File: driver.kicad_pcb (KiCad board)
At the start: 2 copper layers, 53.8 x 69.1 mm, 47 parts, among them J1 Screw_Terminal_01x02, J2 Conn_02x12_Odd_Even, Q10 Q_NMOS_GDSD, Q11 Q_NMOS_GDSD, Q12 Q_NMOS_GDSD, Q13 Q_NMOS_GDSD, Q14 Q_NMOS_GDSD, Q15 Q_NMOS_GDSD, Q16 Q_NMOS_GDSD, Q17 IRF9Z34 PMOS_DGS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

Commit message: Remove reset button, finalize capacitor sizes
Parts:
- removed R8: 10K, Resistor_SMD:R_0805_2012Metric_Pad1.15x1.40mm_HandSolder
- removed SW1: SW_Push, Button_Switch_SMD:SW_SPST_B3S-1000
- C1: value 0.1uF -> 1uF 25V; footprint Capacitor_SMD:C_1210_3225Metric_Pad1.42x2.65mm_HandSolder -> Capacitor_SMD:C_1206_3216Metric_Pad1.42x1.75mm_HandSolder
- C2: value 1uF -> 47uF 60V; footprint Capacitor_THT:CP_Radial_D8.0mm_P3.80mm -> Capacitor_THT:CP_Radial_D6.3mm_P2.50mm
- C3: value 1uF 60V -> 47uF 60V; footprint Capacitor_THT:CP_Radial_D8.0mm_P3.80mm -> Capacitor_THT:CP_Radial_D6.3mm_P2.50mm
- moved C3 3.18 mm to (86.4, 79.5), turned to 90 degrees
- moved C1 2.87 mm to (113.5, 83.8), turned to 180 degrees
- moved C2 0.80 mm to (123.4, 79.5)
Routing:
- net VCC: track 98.7 -> 90.5 mm, vias 0 -> 1
- net 28V: track 103.8 -> 106.0 mm

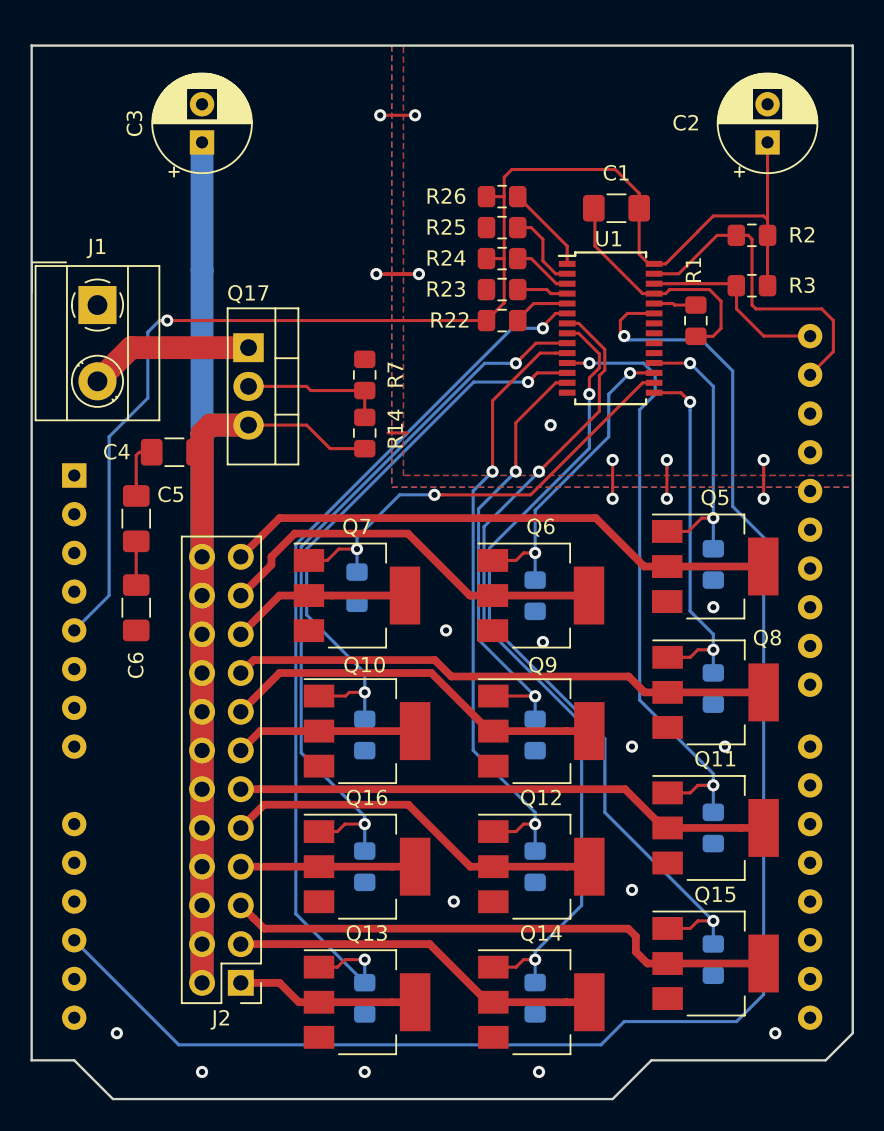
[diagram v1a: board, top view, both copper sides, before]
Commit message: resistor value/footprint changes and associated routing changes
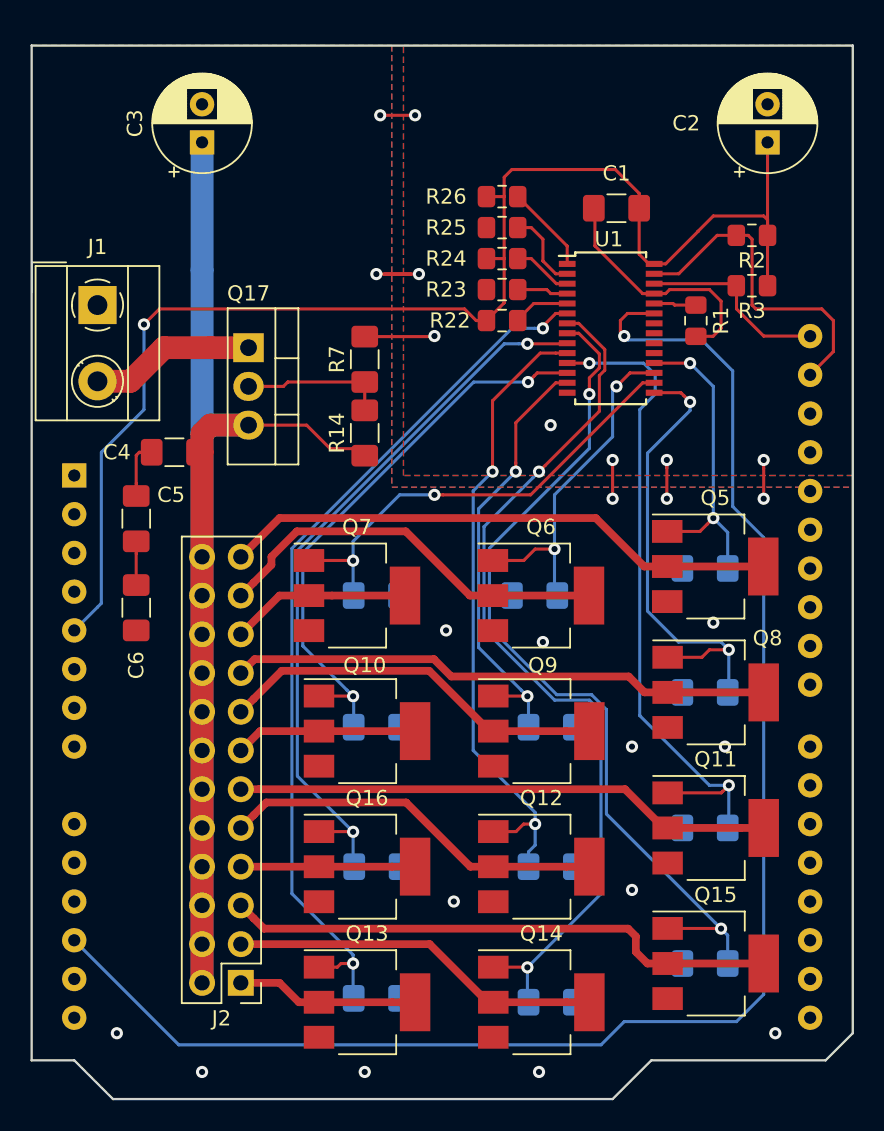
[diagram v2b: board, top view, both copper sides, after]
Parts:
- R1, R2, R22, R23, R24, R25, R26, R3: value 10K -> 1K
- R10, R11, R12, R13, R14, R18, R19, R20, R21, R4, R5, R6, R9: footprint Resistor_SMD:R_0805_2012Metric_Pad1.15x1.40mm_HandSolder -> Resistor_SMD:R_1206_3216Metric_Pad1.42x1.75mm_HandSolder
- R7: value 18K -> 18k1%; footprint Resistor_SMD:R_0805_2012Metric_Pad1.15x1.40mm_HandSolder -> Resistor_SMD:R_1206_3216Metric_Pad1.42x1.75mm_HandSolder
- moved R20 1.37 mm to (97.8, 109.2), turned to 0 degrees
- moved R13 1.17 mm to (109.3, 117.9), turned to 0 degrees
- moved R5 1.08 mm to (109.3, 135.9), turned to 0 degrees
- moved R10 1.05 mm to (109.3, 127.0), turned to 0 degrees
- moved R7 1.03 mm to (97.0, 93.7)
- moved R12 0.92 mm to (97.8, 117.9), turned to 0 degrees
- moved R9 0.80 mm to (97.8, 127.0), turned to 0 degrees
- moved R4 0.76 mm to (97.8, 135.6), turned to 0 degrees
- moved R18 0.60 mm to (119.3, 107.4), turned to 180 degrees
- moved R21 0.60 mm to (119.3, 115.6), turned to 180 degrees
- moved R6 0.60 mm to (119.3, 133.3), turned to 180 degrees
- moved R11 0.54 mm to (119.3, 124.5), turned to 180 degrees
- turned R19 to 180 degrees
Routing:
- net /PWM8: track 24.2 -> 30.9 mm
- net GND: track 32.2 -> 35.5 mm, vias 23 -> 24
- net /PWM2: track 53.6 -> 56.9 mm
- net /PWM5: track 40.4 -> 43.6 mm
- net /PWM1: track 54.8 -> 58.0 mm
- net /PWM10: track 21.0 -> 22.7 mm
- net /PWM11: track 18.6 -> 20.2 mm
- net /PWM0: track 59.8 -> 58.4 mm
- net /PWM4: track 40.9 -> 42.1 mm
- net /PWM9: track 29.4 -> 30.5 mm
- net VCC: track 90.5 -> 91.6 mm
- net Net-(Q17-Pad2): track 9.49 -> 10.1 mm

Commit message: routing and placement
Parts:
- moved R22 13.9 mm to (103.1, 77.6), turned to 90 degrees
- moved R26 12.1 mm to (116.8, 77.6), turned to 90 degrees
- moved R23 11.6 mm to (106.6, 77.6), turned to 90 degrees
- moved R25 10.5 mm to (113.4, 77.6), turned to 90 degrees
- moved R24 10.3 mm to (110.0, 77.6), turned to 90 degrees
- moved R1 1.52 mm to (119.9, 92.2)
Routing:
- net Net-(R26-Pad1): track 5.76 -> 17.0 mm
- net Net-(R22-Pad1): track 3.75 -> 15.0 mm
- net Net-(R23-Pad1): track 3.36 -> 13.0 mm
- net Net-(R24-Pad1): track 3.93 -> 13.5 mm
- net Net-(R25-Pad1): track 5.34 -> 14.0 mm
- net GND: track 35.5 -> 27.0 mm, vias 24 -> 29
- net /PWM10: track 22.7 -> 30.2 mm
- net /~OE: track 102.7 -> 98.0 mm
- net /PWM8: track 30.9 -> 26.3 mm
- net VCC: track 91.6 -> 96.0 mm
- net /PWM1: track 58.0 -> 62.0 mm
- net Net-(R1-Pad1): track 2.78 -> 5.05 mm
- net /PWM2: track 56.9 -> 59.0 mm
- net /PWM4: track 42.1 -> 43.8 mm
- net /PWM5: track 43.6 -> 45.4 mm
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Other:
- board text added: "Heater Drver Board Jacob Killelea"
